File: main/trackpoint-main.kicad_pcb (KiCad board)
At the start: 2 copper layers, 27.5 x 35 mm, 28 parts, among them P1 CONN_10, P2 CONN_5, P3 CONN_8, SW1 CMI126603D08, SW2 CMI126603D08, U1 MKL03Z32VFK4, U4 ESD

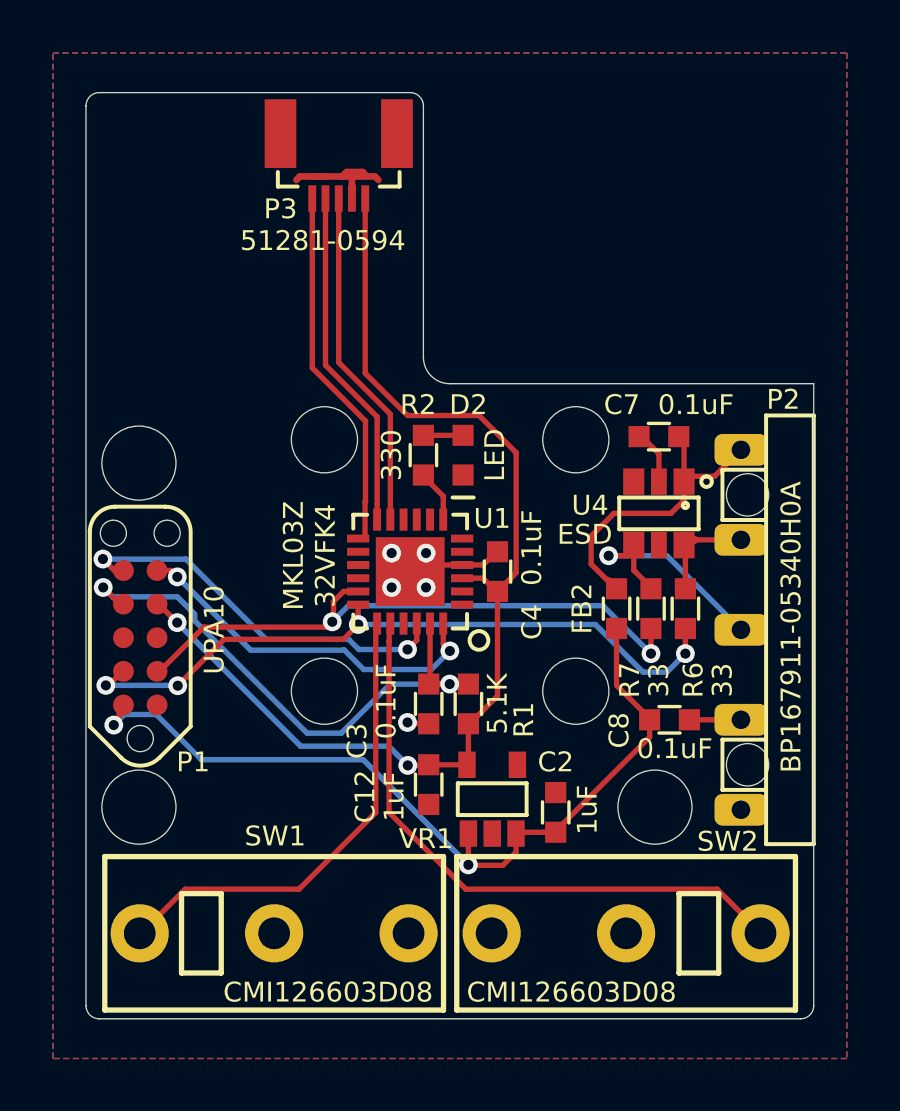
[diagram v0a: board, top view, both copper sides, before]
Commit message: Update PCB based on CAD.
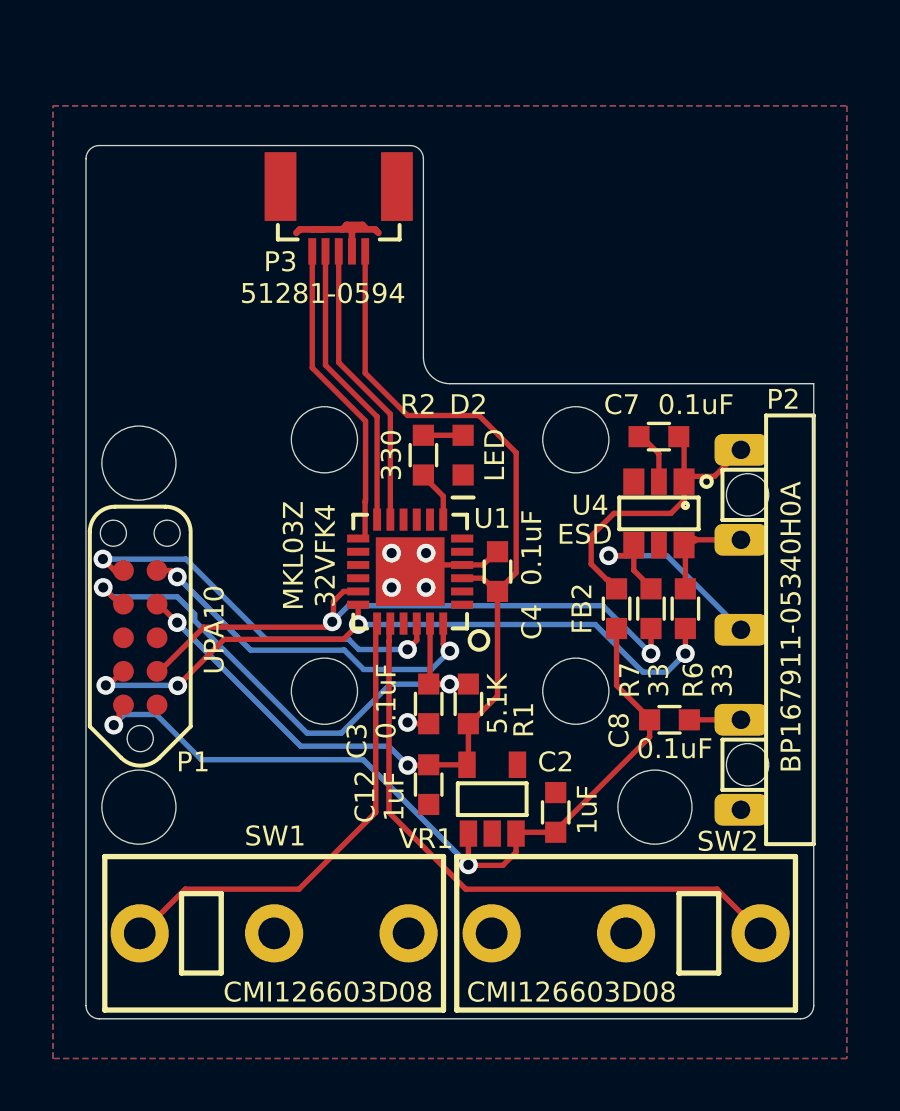
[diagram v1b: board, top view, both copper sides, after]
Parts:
- moved G*** 2.00 mm to (198.6, 116.6)
- moved P3 2.00 mm to (201.8, 114.5)
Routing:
- net /TP_RST: track 12.9 -> 10.7 mm
- net /CLK: track 12.9 -> 10.7 mm
- net /DATA: track 13.8 -> 11.7 mm
- net +3V3: track 40.9 -> 38.8 mm
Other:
- board size 27.5 x 35 mm -> 27.5 x 33 mm

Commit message: Bump PCB version to 2.1.0
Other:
- board text added: "PCB ID: trackpoint_main_2.1.0"
- board text removed: "PCB ID: trackpoint_main_2.0.0"
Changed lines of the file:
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@@
   (title_block
     (title "UHK Trackpoint Module")
-    (rev 2.0.0)
+    (rev 2.1.0)
     (company "Ultimate Gadget Laboratories Kft.")
   )
@@
     (effects (font (size 0.75 0.75) (thickness 0.15)))
   )
-  (gr_text "PCB ID: trackpoint_main_2.0.0" (at 206.1 146.5) (layer B.SilkS)
+  (gr_text "PCB ID: trackpoint_main_2.1.0" (at 206.1 146.5) (layer B.SilkS)
     (effects (font (size 0.75 0.75) (thickness 0.15)) (justify mirror))
   )

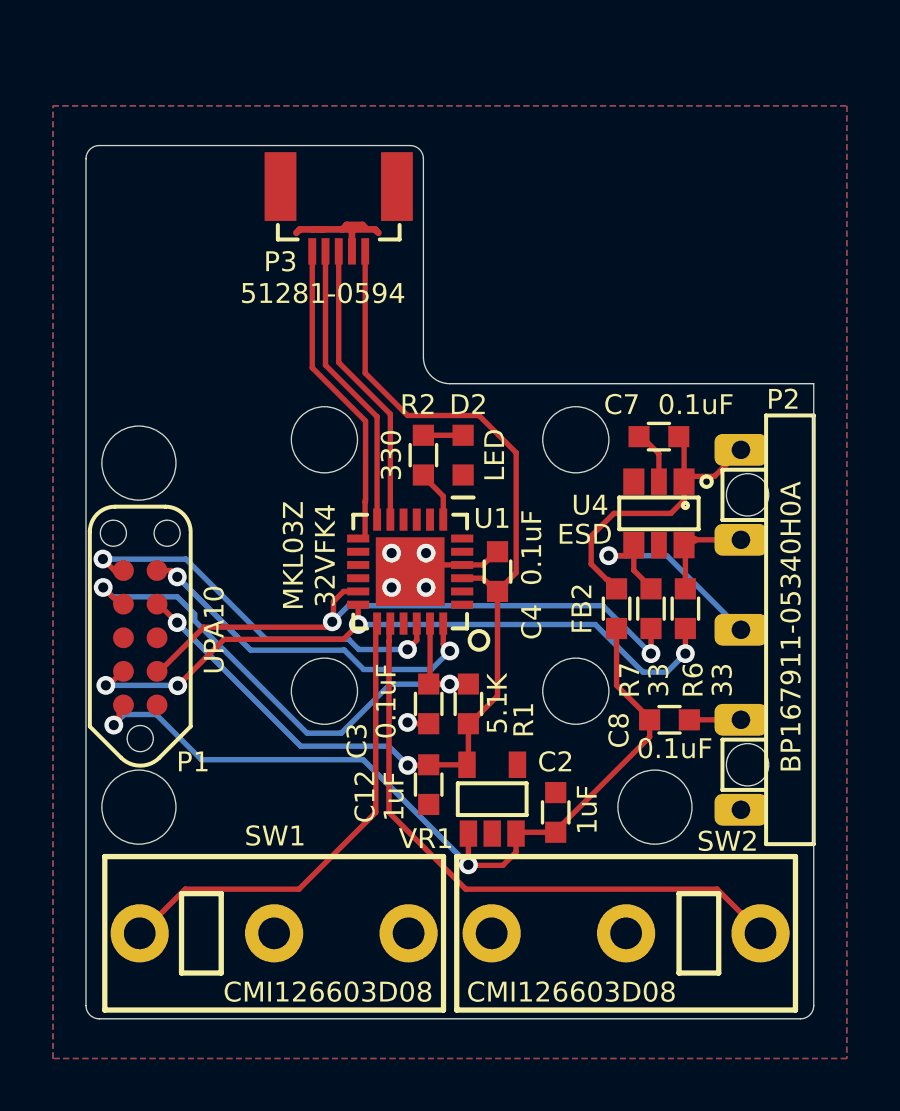
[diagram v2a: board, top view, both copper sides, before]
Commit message: Optimize silk screen for AOI and bump version to 2.1.1
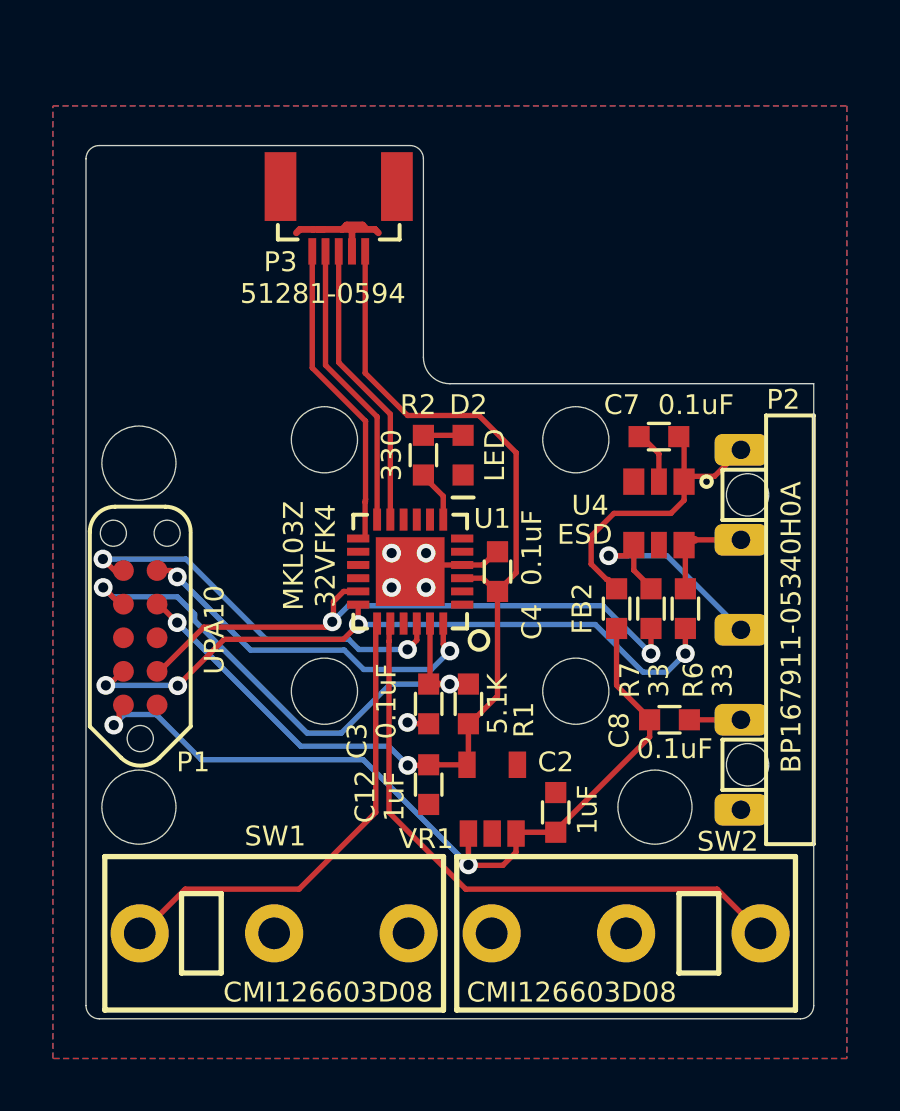
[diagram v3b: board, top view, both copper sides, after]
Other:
- board text added: "PCB ID: trackpoint_main_2.1.1"
- board text removed: "PCB ID: trackpoint_main_2.1.0"
